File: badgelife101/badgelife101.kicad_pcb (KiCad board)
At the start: 2 copper layers, 43.8 x 39.8 mm, 14 parts

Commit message: partial
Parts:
- moved D4 2.12 mm to (142.0, 106.0)
- moved D1 1.95 mm to (123.6, 74.0)
- moved D3 1.86 mm to (123.6, 106.0)
- moved D5 1.80 mm to (114.2, 89.6)
- moved D2 1.77 mm to (141.8, 73.8)
- moved D6 1.60 mm to (151.4, 90.0)

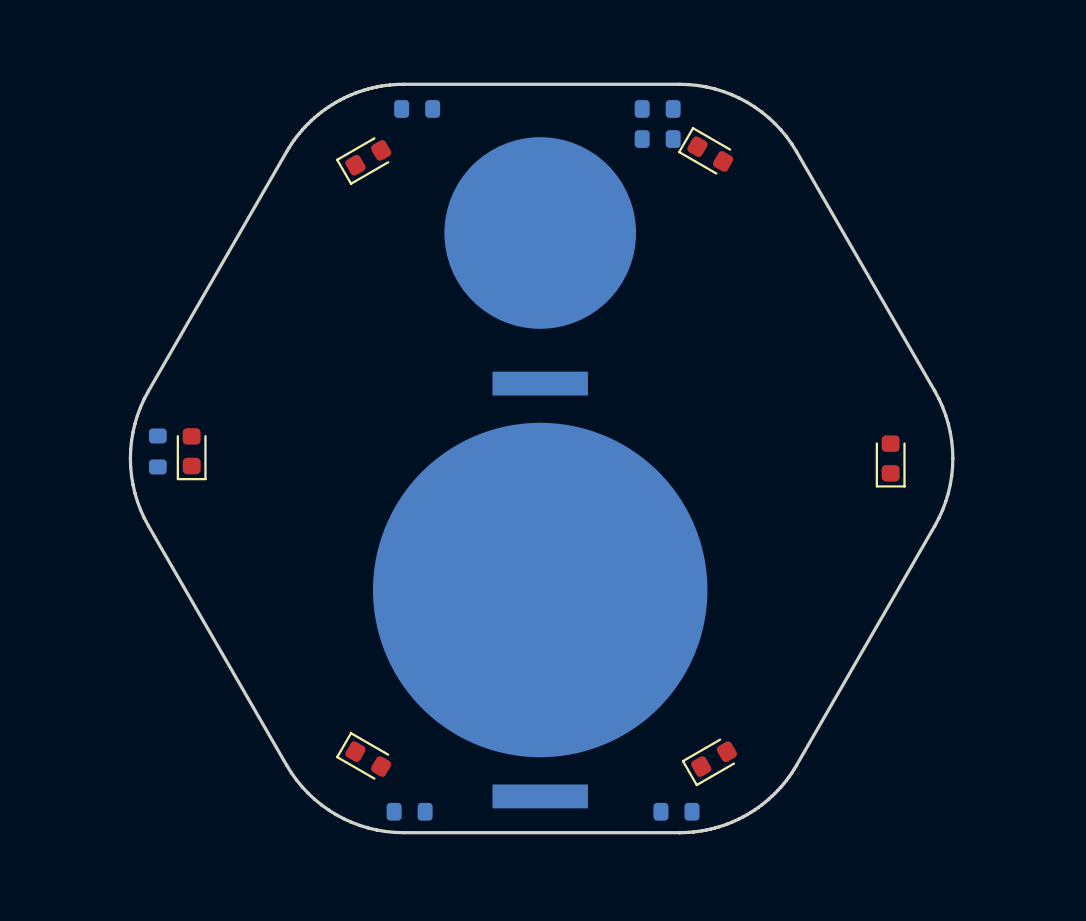
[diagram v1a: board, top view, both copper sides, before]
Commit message: Copper to the edge
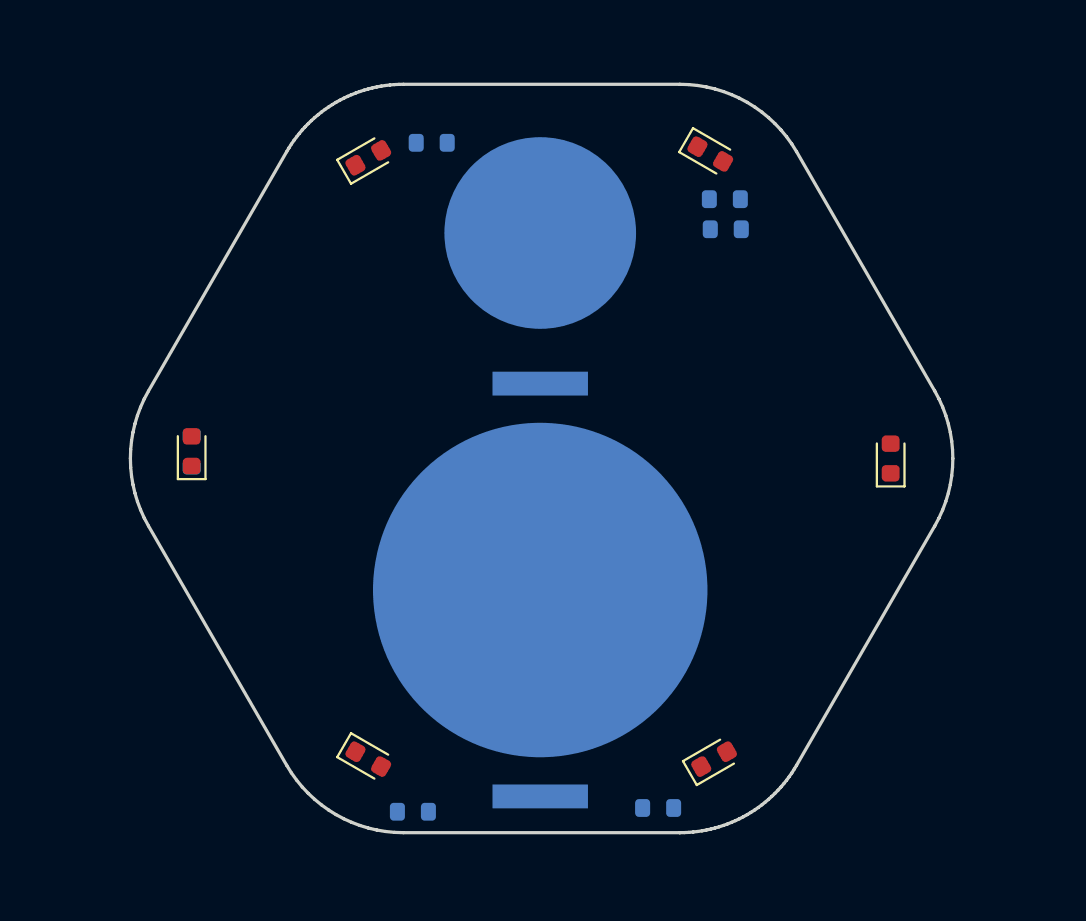
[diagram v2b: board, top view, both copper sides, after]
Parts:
- moved R6 6.02 mm to (142.6, 77.8)
- moved R2 5.99 mm to (142.6, 76.2)
- moved R1 1.96 mm to (127.0, 73.2)
- moved R5 1.80 mm to (114.2, 89.6)
- moved R4 1.00 mm to (139.0, 108.6)
- moved R3 0.17 mm to (126.0, 108.8)

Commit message: MVP
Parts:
- turned D4 to -150 degrees
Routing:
- net VCC: track 0.00 -> 84.0 mm
- net GND: track 0.00 -> 46.3 mm, vias 0 -> 3
- net Net-(D6-A): track 0.00 -> 14.7 mm, vias 0 -> 1
- net Net-(D4-A): track 0.00 -> 3.00 mm, vias 0 -> 1
- net Net-(D3-A): track 0.00 -> 2.83 mm, vias 0 -> 1
- net Net-(D2-A): track 0.00 -> 2.73 mm, vias 0 -> 1
- net Net-(D1-A): track 0.00 -> 2.20 mm, vias 0 -> 1
- net Net-(D5-A): track 0.00 -> 1.62 mm, vias 0 -> 1
- added copper zone on F.Cu, net GND
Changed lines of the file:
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@@
   )
   (footprint "LED_SMD:LED_0603_1608Metric" (layer "F.Cu")
-    (at 142 106 30)
+    (at 142 106 -150)
     (descr "LED SMD 0603 (1608 Metric), square (rectangular) end terminal, IPC_7351 nominal, (Body size source: http://www.tortai-tech.com/upload/download/2011102023233369053.pdf), generated with kicad-footprint-generator")
     (tags "LED")
@@
     (fp_line (start 0.8 0.4) (end 0.8 -0.4)
       (stroke (width 0.1) (type solid)) (layer "F.Fab"))
-    (pad "1" smd roundrect (at -0.7875 0 30) (size 0.875 0.95) (layers "F.Cu" "F.Paste" "F.Mask") (roundrect_rratio 0.25)
+    (pad "1" smd roundrect (at -0.7875 0 210) (size 0.875 0.95) (layers "F.Cu" "F.Paste" "F.Mask") (roundrect_rratio 0.25)
       (net 2 "GND") (pinfunction "K") (pintype "passive"))
-    (pad "2" smd roundrect (at 0.7875 0 30) (size 0.875 0.95) (layers "F.Cu" "F.Paste" "F.Mask") (roundrect_rratio 0.25)
+    (pad "2" smd roundrect (at 0.7875 0 210) (size 0.875 0.95) (layers "F.Cu" "F.Paste" "F.Mask") (roundrect_rratio 0.25)
       (net 6 "Net-(D4-A)") (pinfunction "A") (pintype "passive"))
     (model "${KICAD6_3DMODEL_DIR}/LED_SMD.3dshapes/LED_0603_1608Metric.wrl"
@@
     (property "ki_keywords" "R resistor")
     (attr smd)
-    (fp_text reference "R4" (at 0 1.43) (layer "B.SilkS")
+    (fp_text reference "R4" (at -2.625 0.4) (layer "B.SilkS")
         (effects (font (size 1 1) (thickness 0.15)) (justify mirror))
     )
@@
   (gr_line locked (start 119.508346 106.731981) (end 119.255472 106.325795)
     (stroke (width 0.172347) (type solid)) (layer "Edge.Cuts"))
+  (segment (start 121.75 90.45) (end 121.75 101.95) (width 0.4) (layer "B.Cu") (net 1))
+  (segment (start 127.8 74.6) (end 127.8 73.2) (width 0.4) (layer "B.Cu") (net 1))
+  (segment (start 137.585 107.985) (end 138.2 108.6) (width 0.4) (layer "B.Cu") (net 1))
+  (segment (start 121.75 101.95) (end 126.8 107) (width 0.4) (layer "B.Cu") (net 1))
+  (segment (start 126.185 86.015) (end 121.75 90.45) (width 0.4) (layer "B.Cu") (net 1))
+  (segment (start 132.75 86.015) (end 126.185 86.015) (width 0.4) (layer "B.Cu") (net 1))
+  (segment (start 126.185 86.015) (end 126.185 76.215) (width 0.4) (layer "B.Cu") (net 1))
+  (segment (start 132.75 107.985) (end 137.585 107.985) (width 0.4) (layer "B.Cu") (net 1))
+  (segment (start 141.75 76.2) (end 141.75 77.75) (width 0.4) (layer "B.Cu") (net 1))
+  (segment (start 127.8 73.2) (end 128.8 72.2) (width 0.4) (layer "B.Cu") (net 1))
+  (segment (start 126.185 76.215) (end 127.8 74.6) (width 0.4) (layer "B.Cu") (net 1))
+  (segment (start 126.8 107) (end 126.8 108.8) (width 0.4) (layer "B.Cu") (net 1))
+  (segment (start 127.785 107.985) (end 132.75 107.985) (width 0.4) (layer "B.Cu") (net 1))
+  (segment (start 137.75 72.2) (end 141.75 76.2) (width 0.4) (layer "B.Cu") (net 1))
+  (segment (start 126.8 107) (end 127.785 107.985) (width 0.4) (layer "B.Cu") (net 1))
+  (segment (start 121.75 90.45) (end 114.2 90.45) (width 0.4) (layer "B.Cu") (net 1))
+  (segment (start 141.75 77.75) (end 141.8 77.8) (width 0.4) (layer "B.Cu") (net 1))
+  (segment (start 128.8 72.2) (end 137.75 72.2) (width 0.4) (layer "B.Cu") (net 1))
+  (segment (start 151.4 90.7875) (end 151.4 91.8) (width 0.4) (layer "F.Cu") (net 2))
+  (via (at 144.4 84.4) (size 0.7) (drill 0.3) (layers "F.Cu" "B.Cu") (net 2))
+  (via (at 144.6 94.6) (size 0.7) (drill 0.3) (layers "F.Cu" "B.Cu") (net 2))
+  (via (at 151.4 91.8) (size 0.7) (drill 0.3) (layers "F.Cu" "B.Cu") (net 2))
+  (segment (start 137.4 78) (end 132.75 78) (width 0.4) (layer "B.Cu") (net 2))
+  (segment (start 143.8 84.4) (end 144.4 84.4) (width 0.4) (layer "B.Cu") (net 2))
+  (segment (start 132.75 97) (end 141.4 97) (width 0.4) (layer "B.Cu") (net 2))
+  (segment (start 141.4 97) (end 143.8 94.6) (width 0.4) (layer "B.Cu") (net 2))
+  (segment (start 143.8 84.4) (end 137.4 78) (width 0.4) (layer "B.Cu") (net 2))
+  (segment (start 143.8 94.6) (end 144.6 94.6) (width 0.4) (layer "B.Cu") (net 2))
+  (segment (start 148.6 94.6) (end 144.6 94.6) (width 0.4) (layer "B.Cu") (net 2))
+  (segment (start 143.8 94.6) (end 143.8 84.4) (width 0.4) (layer "B.Cu") (net 2))
+  (segment (start 151.4 91.8) (end 148.6 94.6) (width 0.4) (layer "B.Cu") (net 2))
+  (segment (start 124.888245 73) (end 124.281995 73.60625) (width 0.4) (layer "F.Cu") (net 3))
+  (segment (start 125.2 73) (end 124.888245 73) (width 0.4) (layer "F.Cu") (net 3))
+  (via (at 125.2 73) (size 0.7) (drill 0.3) (layers "F.Cu" "B.Cu") (net 3))
+  (segment (start 125.4 73.2) (end 125.2 73) (width 0.4) (layer "B.Cu") (net 3))
+  (segment (start 126.15 73.2) (end 125.4 73.2) (width 0.4) (layer "B.Cu") (net 3))
+  (segment (start 143.6 75) (end 143.288245 75) (width 0.4) (layer "F.Cu") (net 4))
+  (segment (start 143.288245 75) (end 142.481995 74.19375) (width 0.4) (layer "F.Cu") (net 4))
+  (via (at 143.6 75) (size 0.7) (drill 0.3) (layers "F.Cu" "B.Cu") (net 4))
+  (segment (start 143.4 75.2) (end 143.6 75) (width 0.4) (layer "B.Cu") (net 4))
+  (segment (start 143.4 76.2) (end 143.4 75.2) (width 0.4) (layer "B.Cu") (net 4))
+  (segment (start 124.888245 107) (end 124.281995 106.39375) (width 0.4) (layer "F.Cu") (net 5))
+  (segment (start 125 107) (end 124.888245 107) (width 0.4) (layer "F.Cu") (net 5))
+  (via (at 125 107) (size 0.7) (drill 0.3) (layers "F.Cu" "B.Cu") (net 5))
+  (segment (start 125.15 107.15) (end 125 107) (width 0.4) (layer "B.Cu") (net 5))
+  (segment (start 125.15 108.8) (end 125.15 107.15) (width 0.4) (layer "B.Cu") (net 5))
+  (segment (start 140.511755 107.2) (end 141.318005 106.39375) (width 0.4) (layer "F.Cu") (net 6))
+  (segment (start 140.2 107.2) (end 140.511755 107.2) (width 0.4) (layer "F.Cu") (net 6))
+  (via (at 140.2 107.2) (size 0.7) (drill 0.3) (layers "F.Cu" "B.Cu") (net 6))
+  (segment (start 139.85 107.55) (end 140.2 107.2) (width 0.4) (layer "B.Cu") (net 6))
+  (segment (start 139.85 108.6) (end 139.85 107.55) (width 0.4) (layer "B.Cu") (net 6))
+  (segment (start 114.2 88) (end 114.2 88.825) (width 0.4) (layer "F.Cu") (net 7))
+  (via (at 114.2 88) (size 0.7) (drill 0.3) (layers "F.Cu" "B.Cu") (net 7))
+  (segment (start 114.2 88.8) (end 114.2 88) (width 0.4) (layer "B.Cu") (net 7))
+  (segment (start 151.4 88.2) (end 151.4 89.2125) (width 0.4) (layer "F.Cu") (net 8))
+  (via (at 151.4 88.2) (size 0.7) (drill 0.3) (layers "F.Cu" "B.Cu") (net 8))
+  (segment (start 143.45 77.8) (end 143.45 80.25) (width 0.4) (layer "B.Cu") (net 8))
+  (segment (start 143.45 80.25) (end 151.4 88.2) (width 0.4) (layer "B.Cu") (net 8))
+  (zone (net 2) (net_name "GND") (layer "F.Cu") (hatch edge 0.5)
+    (connect_pads (clearance 0.5))
+    (min_thickness 0.25) (filled_areas_thickness no)
+    (fill yes (thermal_gap 0.5) (thermal_bridge_width 0.25))
+    (polygon
+      (pts
+        (xy 123.2 67.6)
+        (xy 117.4 71)
+        (xy 106 90.8)
+        (xy 119.2 112.6)
+        (xy 145.8 112.6)
+        (xy 159.8 88.6)
+        (xy 145.8 67.6)
+      )
+    )
+  )
   (group "" locked (id 3ee0da48-853f-4de0-8fcc-55310ef4e510)
     (members

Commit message: Update
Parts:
- added REF**: OSHW-Logo2_7.3x6mm_SilkScreen, Symbol:OSHW-Logo2_7.3x6mm_SilkScreen, B.Cu at (146.6, 89.2)
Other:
- board text added: "https://1337.fyi/badgelife101"
